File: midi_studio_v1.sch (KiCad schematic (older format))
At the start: 0 parts

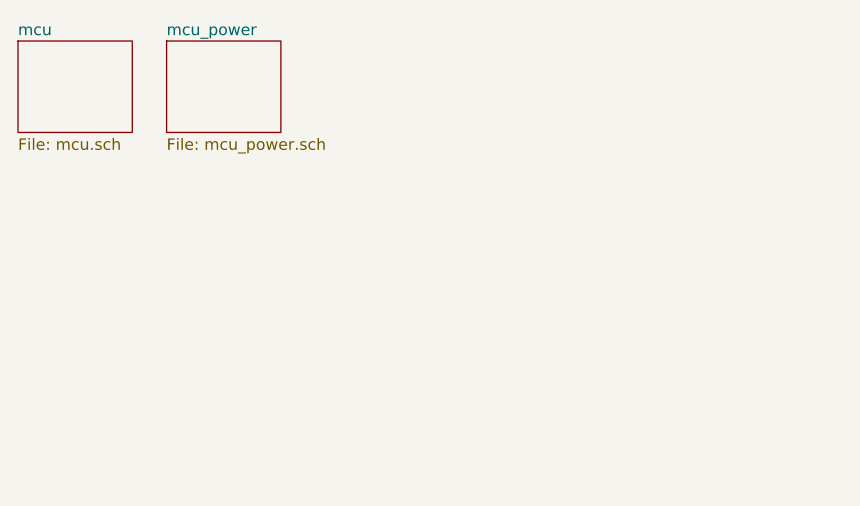
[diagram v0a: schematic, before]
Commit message: Finished MCU power, MCU crystals, started CODEC
Not done CODEC.

Where are the I2S BCLK and LRCLK?
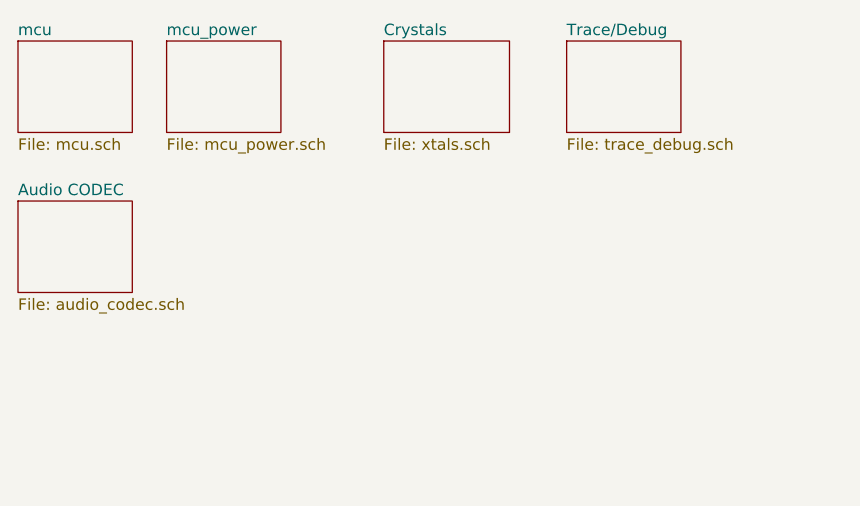
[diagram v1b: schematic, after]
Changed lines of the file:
@@
 $Descr A4 11693 8268
 encoding utf-8
-Sheet 1 3
-Title "MCU"
+Sheet 1 6
+Title "MIDI Studio Schematic"
 Date ""
 Rev ""
@@
 F1 "mcu_power.sch" 50
 $EndSheet
+$Sheet
+S 2700 800  550  400
+U 5CF5F3AC
+F0 "Crystals" 50
+F1 "xtals.sch" 50
+$EndSheet
+$Sheet
+S 3500 800  500  400
+U 5CF60766
+F0 "Trace/Debug" 50
+F1 "trace_debug.sch" 50
+$EndSheet
+$Sheet
+S 1100 1500 500  400
+U 5CF6FA29
+F0 "Audio CODEC" 50
+F1 "audio_codec.sch" 50
+$EndSheet
 $EndSCHEMATC

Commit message: Added SDRAM to schematic
We're assuming we use a unique NBLx for each chip because it seems like if you
actually had a chip with a 32-bit wide data bus, it would have 4 DQM (NBL) pins.
So in this way we simulate a 32-bit wide data bus.
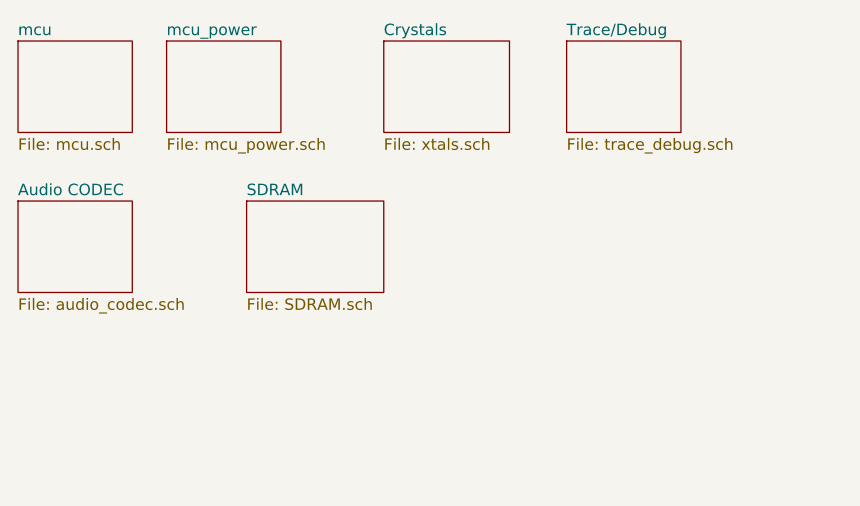
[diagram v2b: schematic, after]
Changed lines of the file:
@@
 $Descr A4 11693 8268
 encoding utf-8
-Sheet 1 6
+Sheet 1 7
 Title "MIDI Studio Schematic"
 Date ""
@@
 F1 "audio_codec.sch" 50
 $EndSheet
+$Sheet
+S 2100 1500 600  400
+U 5CFD50B3
+F0 "SDRAM" 50
+F1 "SDRAM.sch" 50
+$EndSheet
 $EndSCHEMATC

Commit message: Added SD card.
Working on LCD screen. Not yet finished.
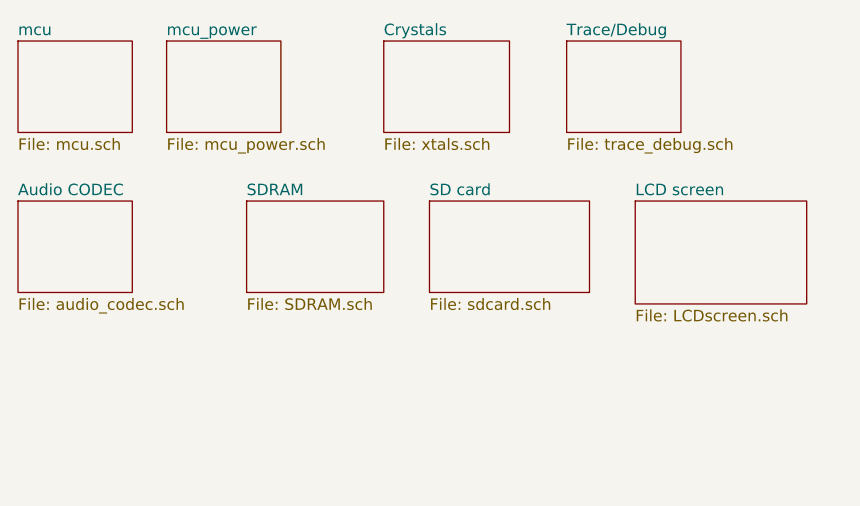
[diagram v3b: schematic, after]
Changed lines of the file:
@@
 $Descr A4 11693 8268
 encoding utf-8
-Sheet 1 7
+Sheet 1 9
 Title "MIDI Studio Schematic"
 Date ""
@@
 F1 "SDRAM.sch" 50
 $EndSheet
+$Sheet
+S 2900 1500 700  400
+U 5CFEB435
+F0 "SD card" 50
+F1 "sdcard.sch" 50
+$EndSheet
+$Sheet
+S 3800 1500 750  450
+U 5CFEBF88
+F0 "LCD screen" 50
+F1 "LCDscreen.sch" 50
+$EndSheet
 $EndSCHEMATC

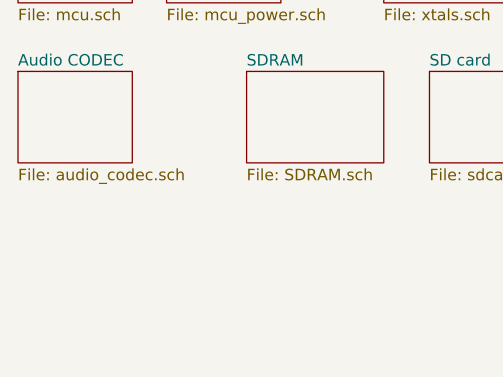
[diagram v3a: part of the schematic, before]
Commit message: Added MIDI
We will split the project into 2 boards:

A larger board will have jacks and extra pins, maybe the voltage regulators.

A smaller daughter card will have all the expensive small stuff: MCU, RAM, CODEC
etc. This also allows us to route differential signals to the MCU (this is
better than transmitting digital signals over long distances, with similar
fidelity, right?)
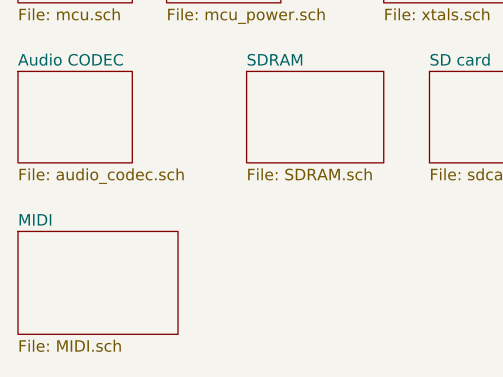
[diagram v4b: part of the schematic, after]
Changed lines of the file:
@@
 $Descr A4 11693 8268
 encoding utf-8
-Sheet 1 9
+Sheet 1 10
 Title "MIDI Studio Schematic"
 Date ""
@@
 F1 "LCDscreen.sch" 50
 $EndSheet
+$Sheet
+S 1100 2200 700  450
+U 5D016BA4
+F0 "MIDI" 50
+F1 "MIDI.sch" 50
+$EndSheet
 $EndSCHEMATC
